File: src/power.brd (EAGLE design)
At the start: 36 x 88.5 mm, 62 parts, among them CON1 PINHEAD_2X02-0877590414, CON2 PINHEAD_2X02-0877590414, CON3 PINHEAD_2X02-0877590414, CON4 PINHEAD_2X02-0877590414, CON5 PINHEAD_2X02-0877590414, CON6 PINHEAD_2X04-SMD-2-MALE, CON7 PINHEAD_2X02-0877590414, IC1 UCC27282-SOIC8, IC2 UCC27282-SOIC8, IC3 UCC27282-SOIC8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

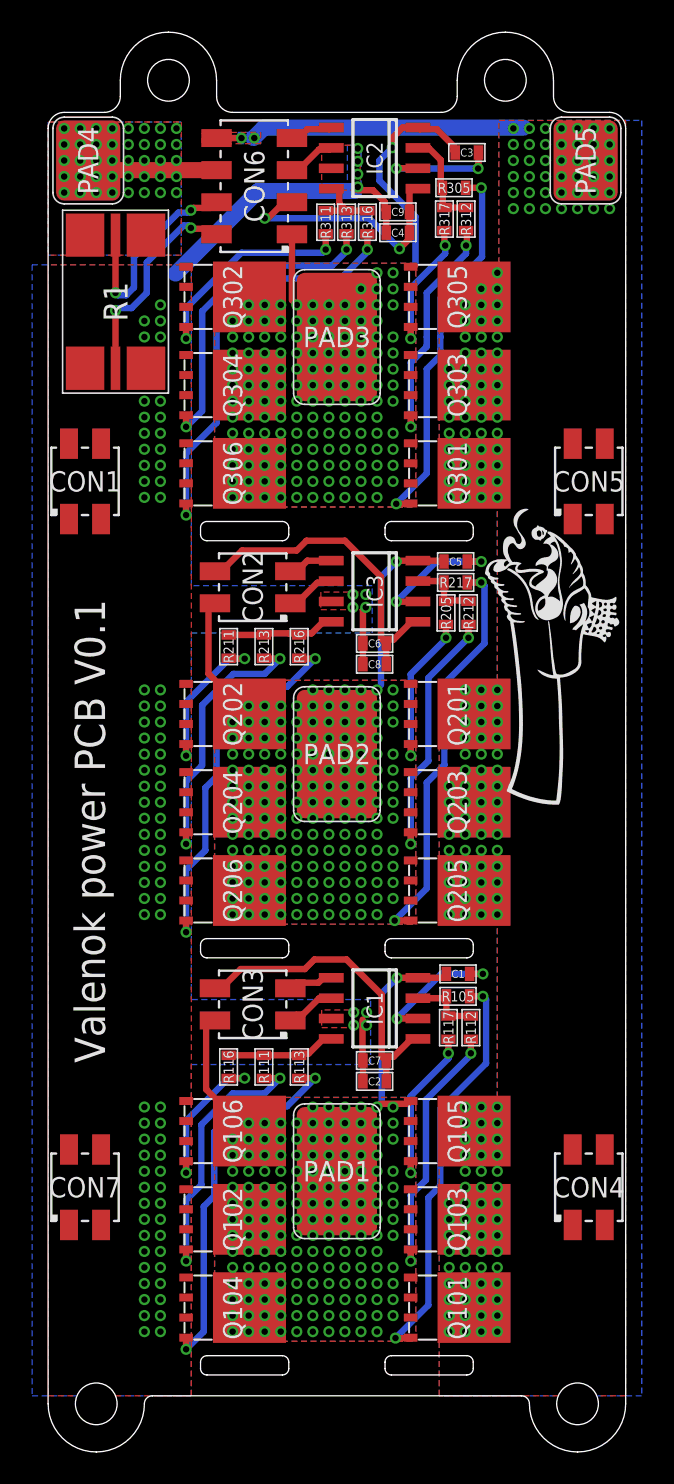
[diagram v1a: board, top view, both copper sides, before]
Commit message: Interpcb connectors updated. Ground problem solved
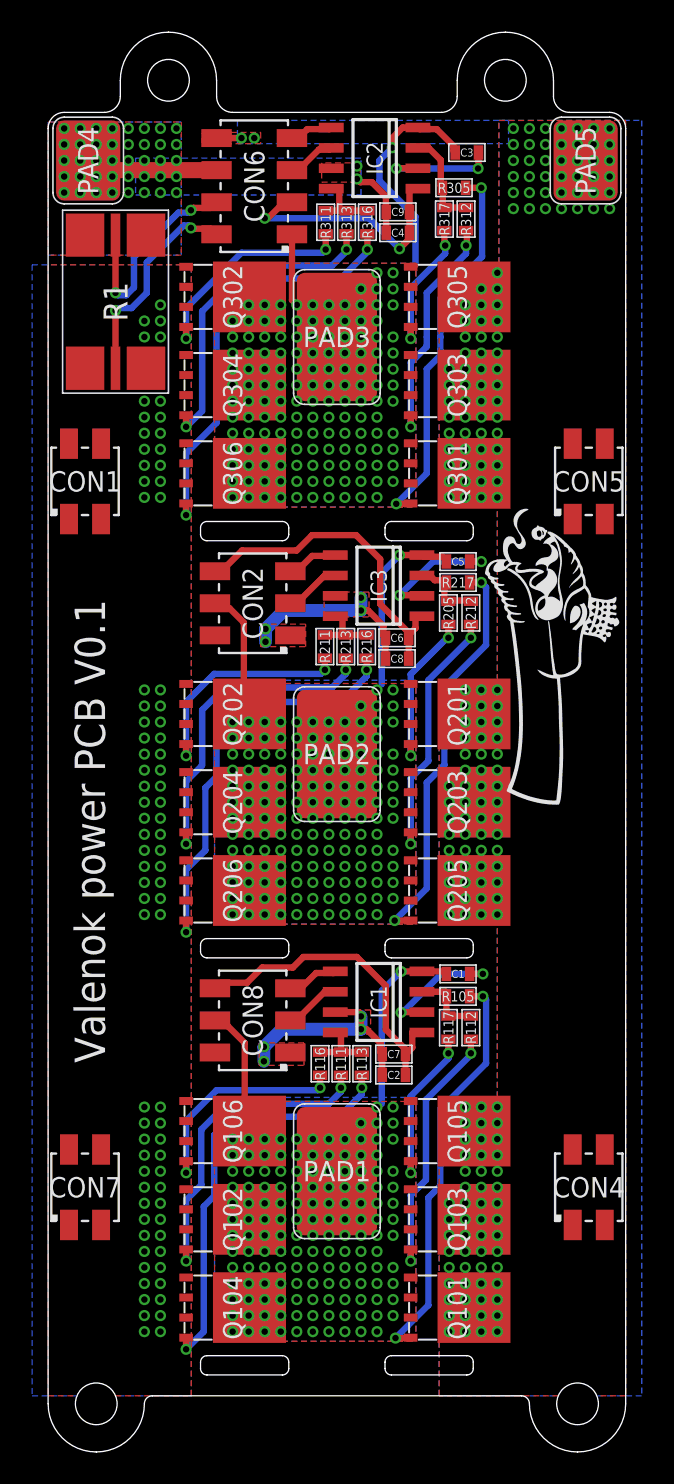
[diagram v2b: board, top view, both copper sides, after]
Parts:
- removed CON3: PINHEAD_2X02-0877590414, pinhead:2X02-SMD-2-MALE
- added CON8: PINHEAD_2X03-0877590614, pinhead:2X03-SMD-2-MALE
- CON2: value PINHEAD_2X02-0877590414 -> PINHEAD_2X03-0877590614; device pinhead:2X02-SMD-2-MALE -> pinhead:2X03-SMD-2-MALE
- moved R211 6.00 mm to (-0.75, 46.7)
- moved R116 5.70 mm to (-1.05, 20.7)
- moved R213 5.10 mm to (0.55, 46.7)
- moved R111 4.80 mm to (0.25, 20.7)
- moved R216 4.20 mm to (1.85, 46.7)
- moved R113 3.91 mm to (1.55, 20.7)
- moved C6 1.44 mm to (3.75, 47.2)
- moved C8 1.44 mm to (3.75, 46.0)
- moved C7 1.26 mm to (3.55, 21.3)
- moved C2 1.26 mm to (3.55, 20.0)
- moved CON2 1.00 mm to (-5.25, 49.4)
- moved IC1 0.47 mm to (2.60, 24.6)
- moved IC3 0.43 mm to (2.60, 50.5)
- moved R205 0.15 mm to (6.95, 48.8)
- moved R212 0.15 mm to (8.35, 48.8)
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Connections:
- new net GND: C2.2, C6.2, C7.2, C8.2, CON2.1, CON8.1, IC1.7, IC3.7
- net 97: now also CON8.6; no longer CON3.4
- net A_IH: now also CON8.5; no longer CON3.3
- net A_IL: now also CON8.3; no longer CON3.1
- net A_PH: now also CON8.4; no longer CON3.2
- net B_IH: now also CON2.5; no longer CON2.3
- net B_IL: now also CON2.3; no longer CON2.1
- net B_PH: now also CON2.4; no longer CON2.2
- net N$4: now also CON2.6; no longer CON2.4
- net PGND: no longer C2.2, C4.2, C6.2, C7.2, C8.2, C9.2, IC1.7, IC2.7, IC3.7
- net VBAT-: now also C4.2, C9.2, IC2.7
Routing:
- net GND: track 0.00 -> 25.9 mm, vias 0 -> 8
- net PGND: track 25.1 -> 0.00 mm, vias 91 -> 79
- net VDC: track 21.0 -> 3.11 mm
- net VBAT-: track 8.28 -> 12.8 mm, vias 40 -> 42
- net PHASE_B:N$2: track 9.85 -> 14.3 mm
- net PHASE_A:N$6: track 9.73 -> 13.9 mm
- net PHASE_B:N$4: track 16.9 -> 20.3 mm
- net PHASE_A:N$2: track 16.7 -> 20.0 mm
- net B_GL: track 6.88 -> 4.22 mm
- net PHASE_B:N$6: track 23.8 -> 26.5 mm
- net A_GL: track 6.82 -> 4.17 mm
- net PHASE_A:N$4: track 23.7 -> 26.2 mm
- net A_PH: track 22.1 -> 20.3 mm, vias 157 -> 146
- net B_PH: track 19.3 -> 20.3 mm, vias 157 -> 146
- added copper zone on layer 1, net GND

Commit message: Massive routing update
InterPCB connectors between Cap PCB and power PCB replaced with bigger ones
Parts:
- CON1, CON4, CON5, CON7: value PINHEAD_2X02-0877590414 -> PINHEAD_2X02-SMD-2.54-MALE; device pinhead:2X02-SMD-2-MALE -> pinhead:PINHEAD_2X02_SMD_MALE_2.54
- moved U$1 4.00 mm to (9.20, 51.3)
- moved CON5 2.06 mm to (15.2, 55.0)
- moved CON1 1.12 mm to (-15.2, 56.0)
- moved CON4 0.50 mm to (15.2, 13.0)
- moved CON7 0.50 mm to (-15.2, 13.0)
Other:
- board text added: "V0.1"
- board text added: "Valenok power PCB"
- board text removed: "Valenok power PCB V0.1"
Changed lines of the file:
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@@
 <setting verticaltext="up"/>
 </settings>
-<grid distance="0.05" unitdist="mm" unit="mm" style="lines" multiple="1" display="yes" altdistance="1" altunitdist="mm" altunit="mm"/>
+<grid distance="1" unitdist="mm" unit="mm" style="lines" multiple="1" display="yes" altdistance="1" altunitdist="mm" altunit="mm"/>
 <layers>
 <layer number="1" name="Top" color="4" fill="1" visible="yes" active="yes"/>
@@
 </layers>
 <board>
-<fusionsync huburn="a.cGVyc29uYWw6dWUyYWE4ZDY4" projecturn="a.cGVyc29uYWw6dWUyYWE4ZDY4IzIwMjAwOTI1MzM2NDYxMjgx" f3durn="urn:adsk.wipprod:dm.lineage:UdILaMCoTQqAY6JzzSHhjw" pcbguid="" lastpulledtime="" lastsyncedchangeguid="" latestrevisionid="c80ee463-d439-426f-ad2b-b43748f011fb" lastsyncedrevisionid="c80ee463-d439-426f-ad2b-b43748f011fb" lastboardhashguid="124f0404-e9a8-8de9-62af-46dde1d5f963" lastpushedtime="2020-11-13T13:51:26Z" linktopcb3d="true"/>
+<fusionsync huburn="a.cGVyc29uYWw6dWUyYWE4ZDY4" projecturn="a.cGVyc29uYWw6dWUyYWE4ZDY4IzIwMjAwOTI1MzM2NDYxMjgx" f3durn="urn:adsk.wipprod:dm.lineage:UdILaMCoTQqAY6JzzSHhjw" pcbguid="" lastpulledtime="" lastsyncedchangeguid="" latestrevisionid="cf7823fd-4bda-43fc-a90e-cc45a5d58e0a" lastsyncedrevisionid="cf7823fd-4bda-43fc-a90e-cc45a5d58e0a" lastboardhashguid="b4dbb701-e8f7-696e-6ea7-af1b2f65365b" lastpushedtime="2020-11-23T15:03:11Z" linktopcb3d="true"/>
 <plain>
 <dimension x1="18" y1="80" x2="18" y2="0" x3="22.000003125" y3="40" textsize="1.778" layer="49"/>
@@
 <wire x1="-10.5" y1="62.5" x2="-10.5" y2="74" width="0.1524" layer="49"/>
 <wire x1="-10.5" y1="74" x2="-17" y2="74" width="0.1524" layer="49"/>
-<text x="-15.4" y="35.2" size="1.9" layer="21" font="vector" ratio="15" rot="R90" align="center">Valenok power PCB V0.1</text>
+<text x="-16.4" y="35.2" size="1.9" layer="21" font="vector" ratio="15" rot="R90" align="center">Valenok power PCB</text>
+<text x="-13.4" y="46.7" size="1.9" layer="21" font="vector" ratio="15" rot="R90" align="center">V0.1</text>
 </plain>
 <attributes>
@@
 <attribute name="TOLERANCE" value="±1%" x="-13.8" y="68.2" size="1.778" layer="27" rot="R270" display="off"/>
 </element>
-<element name="CON1" library="pinhead" library_urn="urn:adsk.eagle:library:2540341" package="2X02-SMD-2-MALE" package3d_urn="urn:adsk.eagle:package:23512771/2" value="PINHEAD_2X02-0877590414" x="-15.7" y="57" smashed="yes" rot="R90">
-<attribute name="DIGIKEY#" value="WM18712-ND" x="-15.7" y="57" size="1.778" layer="27" rot="R90" display="off"/>
-<attribute name="MANF" value="Molex" x="-15.7" y="57" size="1.778" layer="27" rot="R90" display="off"/>
-<attribute name="MANF#" value="0877590414" x="-15.7" y="57" size="1.778" layer="27" rot="R90" display="off"/>
-<attribute name="NAME" x="-15.7" y="57" size="1.27" layer="25" font="vector" ratio="15" align="center"/>
-</element>
-<element name="CON5" library="pinhead" library_urn="urn:adsk.eagle:library:2540341" package="2X02-SMD-2-MALE" package3d_urn="urn:adsk.eagle:package:23512771/2" value="PINHEAD_2X02-0877590414" x="15.7" y="57" smashed="yes" rot="R90">
-<attribute name="DIGIKEY#" value="WM18712-ND" x="15.7" y="57" size="1.778" layer="27" rot="R90" display="off"/>
-<attribute name="MANF" value="Molex" x="15.7" y="57" size="1.778" layer="27" rot="R90" display="off"/>
-<attribute name="MANF#" value="0877590414" x="15.7" y="57" size="1.778" layer="27" rot="R90" display="off"/>
-<attribute name="NAME" x="15.7" y="57" size="1.27" layer="25" font="vector" ratio="15" align="center"/>
+<element name="CON1" library="pinhead" library_urn="urn:adsk.eagle:library:2540341" package="PINHEAD_2X02_SMD_MALE_2.54" package3d_urn="urn:adsk.eagle:package:24450034/3" value="PINHEAD_2X02-SMD-2.54-MALE" x="-15.2" y="56" smashed="yes" rot="R90">
+<attribute name="NAME" x="-15.2" y="56" size="1.27" layer="25" font="vector" ratio="15" align="center"/>
+</element>
+<element name="CON5" library="pinhead" library_urn="urn:adsk.eagle:library:2540341" package="PINHEAD_2X02_SMD_MALE_2.54" package3d_urn="urn:adsk.eagle:package:24450034/3" value="PINHEAD_2X02-SMD-2.54-MALE" x="15.2" y="55" smashed="yes" rot="R90">
+<attribute name="NAME" x="15.2" y="55" size="1.27" layer="25" font="vector" ratio="15" align="center"/>
 </element>
 <element name="CON6" library="pinhead" library_urn="urn:adsk.eagle:library:2540341" package="2X04-SMD-2-MALE" package3d_urn="urn:adsk.eagle:package:23791919/2" value="PINHEAD_2X04-SMD-2-MALE" x="-5.15" y="75.4" smashed="yes" rot="R180">
@@
 <attribute name="NAME" x="-5.15" y="75.4" size="1.27" layer="25" font="vector" ratio="15" rot="R90" align="center"/>
 </element>
-<element name="CON4" library="pinhead" library_urn="urn:adsk.eagle:library:2540341" package="2X02-SMD-2-MALE" package3d_urn="urn:adsk.eagle:package:23512771/2" value="PINHEAD_2X02-0877590414" x="15.7" y="13" smashed="yes" rot="R90">
-<attribute name="DIGIKEY#" value="WM18712-ND" x="16.2" y="13" size="1.778" layer="27" rot="R90" display="off"/>
-<attribute name="MANF" value="Molex" x="16.2" y="13" size="1.778" layer="27" rot="R90" display="off"/>
-<attribute name="MANF#" value="0877590414" x="16.2" y="13" size="1.778" layer="27" rot="R90" display="off"/>
-<attribute name="NAME" x="15.7" y="13" size="1.27" layer="25" font="vector" ratio="15" align="center"/>
-</element>
-<element name="CON7" library="pinhead" library_urn="urn:adsk.eagle:library:2540341" package="2X02-SMD-2-MALE" package3d_urn="urn:adsk.eagle:package:23512771/2" value="PINHEAD_2X02-0877590414" x="-15.7" y="13" smashed="yes" rot="R90">
-<attribute name="DIGIKEY#" value="WM18712-ND" x="-15.7" y="13" size="1.778" layer="27" rot="R90" display="off"/>
-<attribute name="MANF" value="Molex" x="-15.7" y="13" size="1.778" layer="27" rot="R90" display="off"/>
-<attribute name="MANF#" value="0877590414" x="-15.7" y="13" size="1.778" layer="27" rot="R90" display="off"/>
-<attribute name="NAME" x="-15.7" y="13" size="1.27" layer="25" font="vector" ratio="15" align="center"/>
+<element name="CON4" library="pinhead" library_urn="urn:adsk.eagle:library:2540341" package="PINHEAD_2X02_SMD_MALE_2.54" package3d_urn="urn:adsk.eagle:package:24450034/3" value="PINHEAD_2X02-SMD-2.54-MALE" x="15.2" y="13" smashed="yes" rot="R90">
+<attribute name="NAME" x="15.2" y="13" size="1.27" layer="25" font="vector" ratio="15" align="center"/>
+</element>
+<element name="CON7" library="pinhead" library_urn="urn:adsk.eagle:library:2540341" package="PINHEAD_2X02_SMD_MALE_2.54" package3d_urn="urn:adsk.eagle:package:24450034/3" value="PINHEAD_2X02-SMD-2.54-MALE" x="-15.2" y="13" smashed="yes" rot="R90">
+<attribute name="NAME" x="-15.2" y="13" size="1.27" layer="25" font="vector" ratio="15" align="center"/>
 </element>
 <element name="C7" library="rc" library_urn="urn:adsk.eagle:library:2539423" package="C0603" package3d_urn="urn:adsk.eagle:package:2539457/2" value="1000pF" x="3.55" y="21.3" smashed="yes" rot="R180">
@@
 <attribute name="VOLTAGE" value="50V" x="3.8" y="73.8" size="1.778" layer="27" rot="R180" display="off"/>
 </element>
-<element name="U$1" library="logo" library_urn="urn:adsk.eagle:library:6668987" package="DRAGON-18X7" package3d_urn="urn:adsk.eagle:package:11612848/1" value="" x="9.2" y="55.3" smashed="yes" rot="R270"/>
+<element name="U$1" library="logo" library_urn="urn:adsk.eagle:library:6668987" package="DRAGON-18X7" package3d_urn="urn:adsk.eagle:package:11612848/1" value="" x="9.2" y="51.3" smashed="yes" rot="R270"/>
 <element name="CON8" library="pinhead" library_urn="urn:adsk.eagle:library:2540341" package="2X03-SMD-2-MALE" package3d_urn="urn:adsk.eagle:package:23512772/2" value="PINHEAD_2X03-0877590614" x="-5.25" y="23.4" smashed="yes" rot="R180">
 <attribute name="DIGIKEY#" value="WM18713-ND" x="-5.25" y="23.4" size="1.778" layer="27" rot="R180" display="off"/>
